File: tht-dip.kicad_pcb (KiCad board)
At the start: 2 copper layers, 100 x 49 mm, 56 parts, among them J1 Conn_01x01_Female, J10 Conn_01x01_Female, J2 Conn_01x01_Female, J3 Conn_01x01_Female, J4 Conn_01x01_Female, J5 Conn_01x01_Female, J6 Conn_01x01_Female, J7 Conn_01x01_Female, J8 Conn_01x01_Female, J9 Conn_01x01_Female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

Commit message: Add files via upload
updated files.
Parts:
- moved J8 1.00 mm to (39.0, 76.0), turned to 90 degrees

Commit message: Add files via upload
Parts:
- removed R19, R27: 8K, Resistor_THT:R_Axial_DIN0204_L3.6mm_D1.6mm_P5.08mm_Horizontal
- removed the REF** at (123.0, 70.2)
- added REF**: OSHW-Logo2_14.6x12mm_SilkScreen, Symbol:OSHW-Logo2_14.6x12mm_SilkScreen, F.Cu at (122.8, 69.5)
- R13, R21: value 2K -> 3K
- R14, R22: value 3K -> 4K
- R15, R23: value 4K -> 5K
- R16, R24: value 5K -> 6K
- R17, R25: value 6K -> 7K
- R18, R26: value 7K -> 8K
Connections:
- SW1 pad 9: Net-(R19-Pad2) -> (no net)
- SW2 pad 9: Net-(R27-Pad2) -> (no net)
- U1 pad 1: Net-(U1-Pad1) -> (no net)
- U1 pad 5: Net-(U1-Pad5) -> (no net)
- U1 pad 8: Net-(U1-Pad8) -> (no net)
- U2 pad 1: Net-(U2-Pad1) -> (no net)
- U2 pad 5: Net-(U2-Pad5) -> (no net)
- U2 pad 8: Net-(U2-Pad8) -> (no net)
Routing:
- net Net-(R27-Pad2): track 3.04 -> 0.00 mm
- net Net-(R19-Pad2): track 2.86 -> 0.00 mm
- net ResOUT: vias 0 -> 1

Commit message: Add files via upload
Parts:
- C3: footprint Capacitor_THT:C_Disc_D5.0mm_W2.5mm_P2.50mm -> Capacitor_THT:CP_Radial_D6.3mm_P2.50mm
- moved C3 45.2 mm to (114.5, 55.0), turned to 0 degrees
- moved REF** 0.50 mm to (123.2, 69.5)
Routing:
- net VCC: track 183.2 -> 187.7 mm
- net V-: track 202.5 -> 206.7 mm

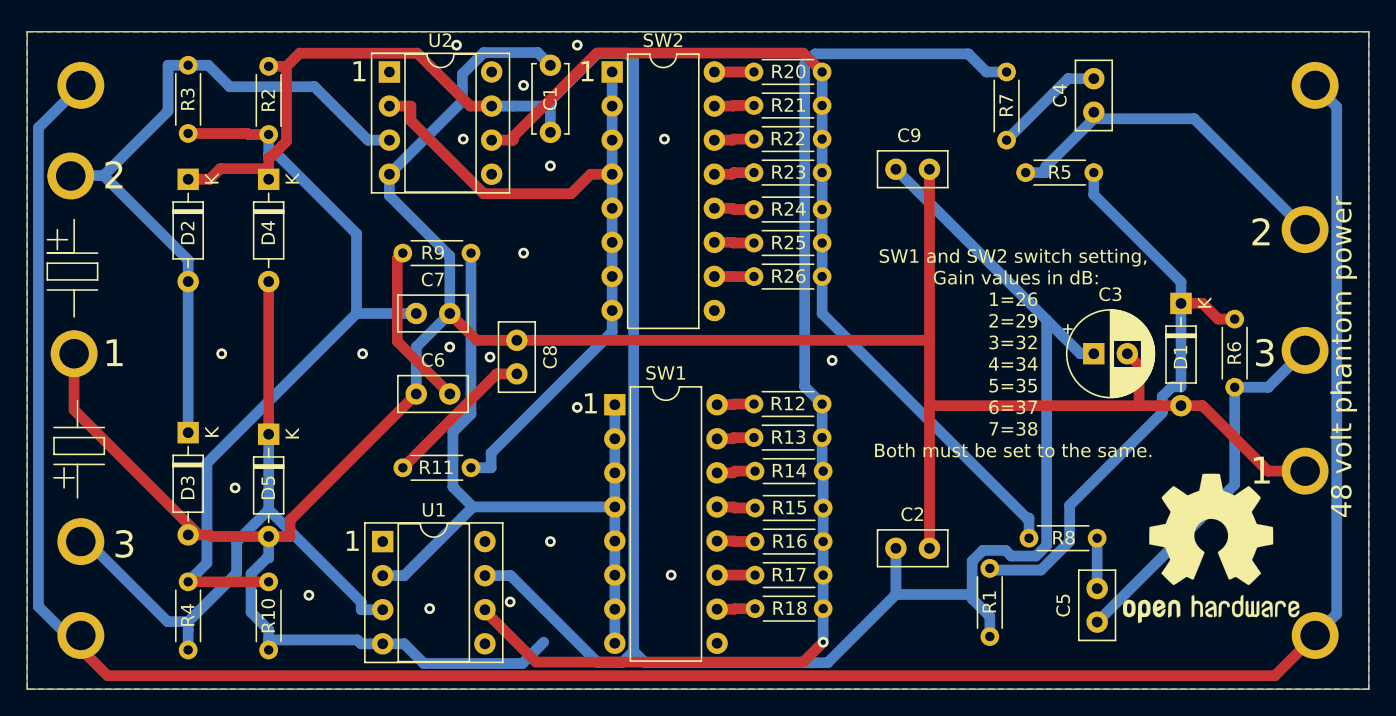
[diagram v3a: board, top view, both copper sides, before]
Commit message: Add files via upload
Updated, with the addition of a 700 ohm resistor.
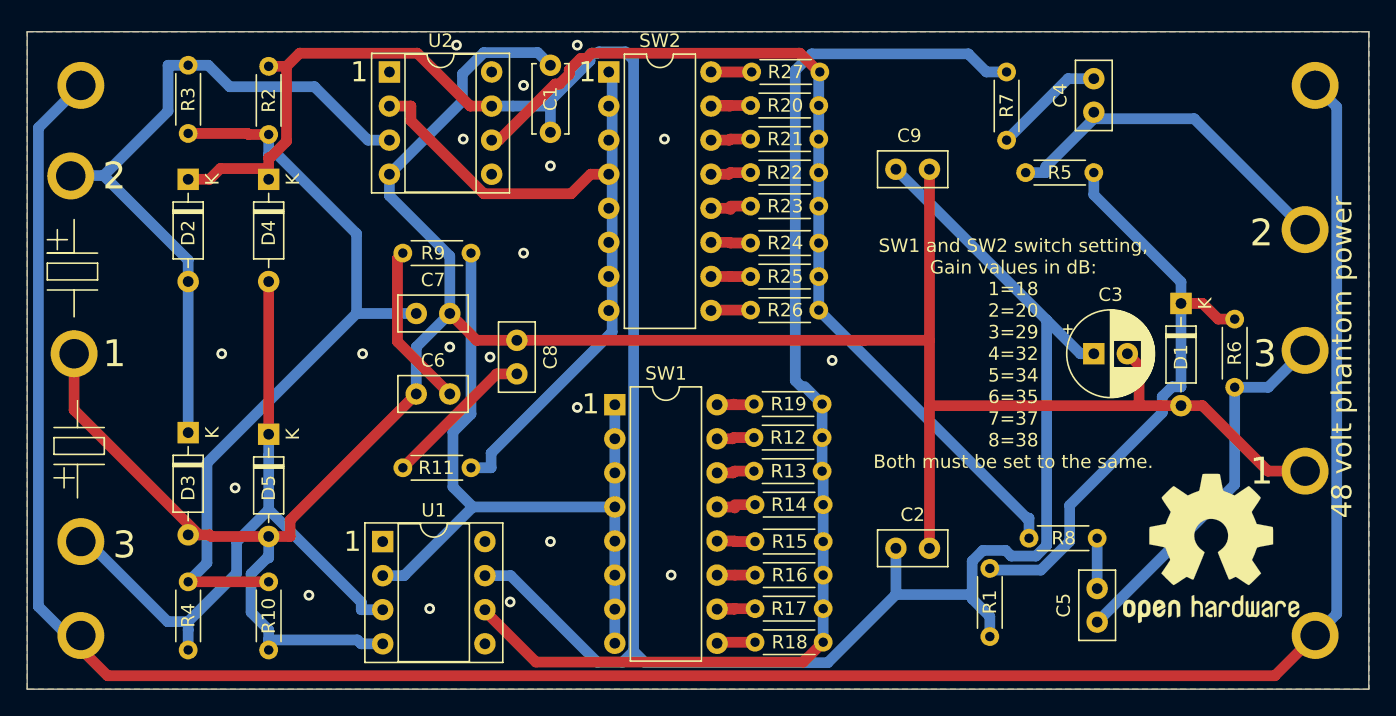
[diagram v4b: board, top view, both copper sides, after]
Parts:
- added R19: 700, Resistor_THT:R_Axial_DIN0204_L3.6mm_D1.6mm_P5.08mm_Horizontal, F.Cu at (94.2, 58.8)
- added R27: 700, Resistor_THT:R_Axial_DIN0204_L3.6mm_D1.6mm_P5.08mm_Horizontal, F.Cu at (94.1, 34.0)
- moved R20 2.51 mm to (94.0, 36.5)
- moved R21 2.51 mm to (94.0, 39.0)
- moved R22 2.51 mm to (94.0, 41.5)
- moved R23 2.51 mm to (94.0, 44.0)
- moved R24 2.51 mm to (94.0, 46.8)
- moved R25 2.51 mm to (94.0, 49.2)
- moved R26 2.51 mm to (94.0, 51.8)
- moved R12 2.50 mm to (94.2, 61.2)
- moved R13 2.50 mm to (94.2, 63.8)
- moved R14 2.50 mm to (94.3, 66.2)
- moved R15 2.50 mm to (94.3, 69.0)
- moved R16 2.50 mm to (94.3, 71.5)
- moved R17 2.50 mm to (94.3, 74.0)
- moved R18 2.50 mm to (94.3, 76.5)
- moved SW2 0.25 mm to (78.3, 34.0)
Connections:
- SW1 pad 10: Net-(R18-Pad2) -> Net-(R17-Pad2)
- SW1 pad 11: Net-(R17-Pad2) -> Net-(R16-Pad2)
- SW1 pad 12: Net-(R16-Pad2) -> Net-(R15-Pad2)
- SW1 pad 13: Net-(R15-Pad2) -> Net-(R14-Pad2)
- SW1 pad 14: Net-(R14-Pad2) -> Net-(R13-Pad2)
- SW1 pad 15: Net-(R13-Pad2) -> Net-(R12-Pad2)
- SW1 pad 16: Net-(R12-Pad2) -> Net-(R19-Pad2)
- SW1 pad 9: (no net) -> Net-(R18-Pad2)
- SW2 pad 10: Net-(R26-Pad2) -> Net-(R25-Pad2)
- SW2 pad 11: Net-(R25-Pad2) -> Net-(R24-Pad2)
- SW2 pad 12: Net-(R24-Pad2) -> Net-(R23-Pad2)
- SW2 pad 13: Net-(R23-Pad2) -> Net-(R22-Pad2)
- SW2 pad 14: Net-(R22-Pad2) -> Net-(R21-Pad2)
- SW2 pad 15: Net-(R21-Pad2) -> Net-(R20-Pad2)
- SW2 pad 16: Net-(R20-Pad2) -> Net-(R27-Pad2)
- SW2 pad 9: (no net) -> Net-(R26-Pad2)
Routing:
- net V-: track 206.7 -> 193.5 mm
- net Net-(R27-Pad2): track 0.00 -> 3.03 mm
- net Net-(R19-Pad2): track 0.00 -> 2.84 mm
- net Net-(R20-Pad2): track 2.95 -> 4.42 mm
- net Net-(R17-Pad2): track 2.83 -> 4.18 mm
- net ResOUT: track 87.1 -> 87.7 mm
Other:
- board text added: "SW1 and SW2 switch setting, Gain values in dB: 1=18 2=20 3=29 4=32 5=34 6=35 7=37 8=38 Both must be set to the same."
- board text removed: "SW1 and SW2 switch setting, Gain values in dB: 1=26 2=29 3=32 4=34 5=35 6=37 7=38 Both must be set to the same."

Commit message: Add files via upload
Changed to TL082BCP , less current use.
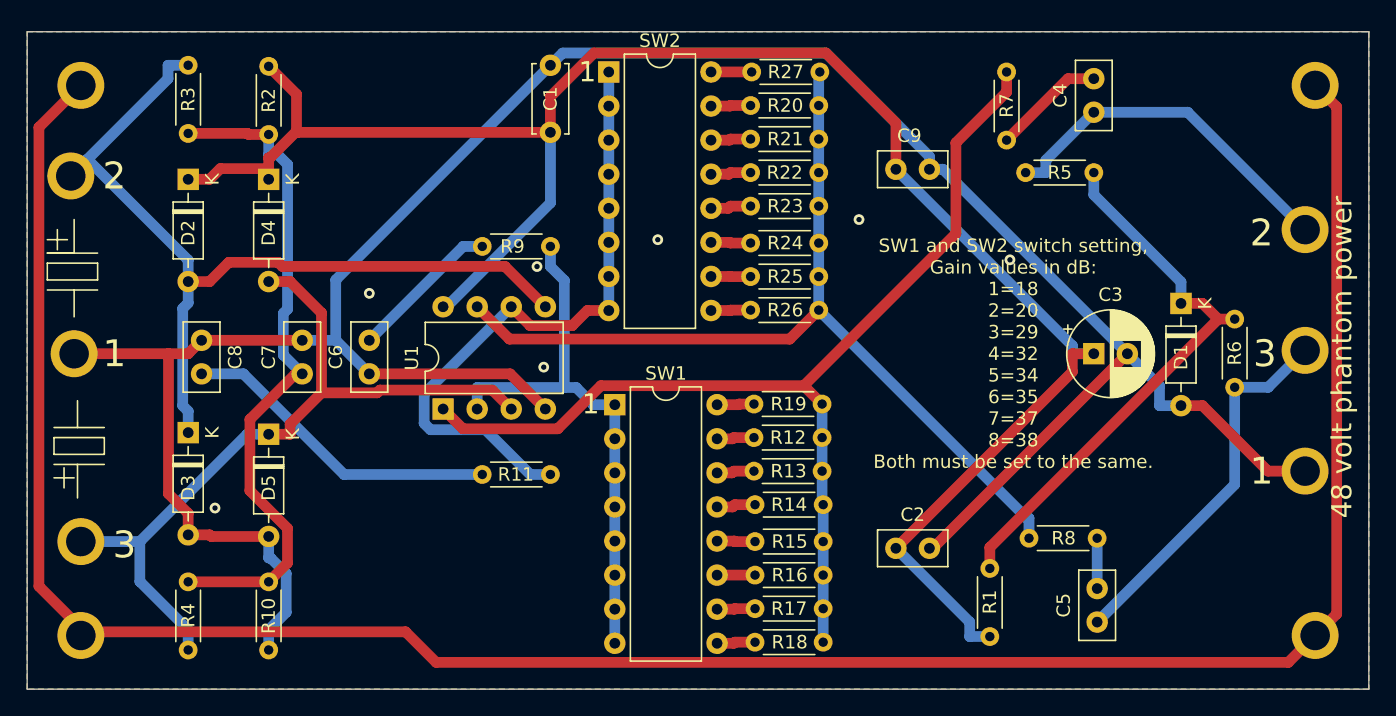
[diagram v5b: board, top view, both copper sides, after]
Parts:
- removed REF**: OSHW-Logo2_14.6x12mm_SilkScreen, Symbol:OSHW-Logo2_14.6x12mm_SilkScreen
- removed U2: NE5534, Package_DIP:DIP-8_W7.62mm_Socket
- D1: value 1N4746A (18V) -> 1N5241B-TR
- U1: value NE5534 -> TL082BCP; footprint Package_DIP:DIP-8_W7.62mm_Socket -> Package_DIP:DIP-8_W7.62mm
- moved C8 23.5 mm to (48.0, 54.0)
- moved U1 10.9 mm to (66.0, 59.1), turned to 90 degrees
- moved C7 9.62 mm to (55.5, 56.5), turned to 90 degrees
- moved R11 5.94 mm to (68.9, 64.0)
- moved R9 5.94 mm to (68.9, 47.0)
- moved C6 3.81 mm to (60.5, 56.5), turned to 90 degrees
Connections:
- U1 pad 1: (no net) -> ResOUT
- U1 pad 5: (no net) -> ind
- U1 pad 6: ResOUT -> ResIN1
- U1 pad 7: VCC -> ResOUT2
- U1 pad 8: (no net) -> VCC
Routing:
- net VCC: track 188.1 -> 140.0 mm
- net ResIN: track 57.3 -> 41.1 mm
- net Net-(C8-Pad2): track 11.4 -> 24.0 mm
- net ind: track 53.3 -> 65.2 mm
- net ResOUT: track 87.7 -> 78.2 mm, vias 1 -> 0
- net Net-(C7-Pad1): track 58.1 -> 50.7 mm
- net V-: track 193.5 -> 186.3 mm
- net ResIN1: track 55.3 -> 48.5 mm
- net Net-(D4-Pad2): track 53.2 -> 58.2 mm
- net Net-(D1-Pad1): track 45.4 -> 42.6 mm
- net Net-(R20-Pad2): track 4.42 -> 2.97 mm
- net Earth: track 181.0 -> 179.6 mm, vias 19 -> 7
- net Net-(R17-Pad2): track 4.18 -> 2.85 mm
- net Net-(C6-Pad2): track 12.3 -> 11.3 mm

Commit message: Add files via upload
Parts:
- removed R12, R20: 1K, Resistor_THT:R_Axial_DIN0204_L3.6mm_D1.6mm_P5.08mm_Horizontal
- removed R13, R21: 3K, Resistor_THT:R_Axial_DIN0204_L3.6mm_D1.6mm_P5.08mm_Horizontal
- removed R14, R22: 4K, Resistor_THT:R_Axial_DIN0204_L3.6mm_D1.6mm_P5.08mm_Horizontal
- removed R15, R23: 5K, Resistor_THT:R_Axial_DIN0204_L3.6mm_D1.6mm_P5.08mm_Horizontal
- removed R16, R24: 6K, Resistor_THT:R_Axial_DIN0204_L3.6mm_D1.6mm_P5.08mm_Horizontal
- removed R17, R25: 7K, Resistor_THT:R_Axial_DIN0204_L3.6mm_D1.6mm_P5.08mm_Horizontal
- removed R18, R26: 8K, Resistor_THT:R_Axial_DIN0204_L3.6mm_D1.6mm_P5.08mm_Horizontal
- removed R19, R27: 700, Resistor_THT:R_Axial_DIN0204_L3.6mm_D1.6mm_P5.08mm_Horizontal
- removed SW1, SW2: JS0108AP4-S, Package_DIP:DIP-16_W7.62mm
- added RV1: R_Potentiometer_Dual, potmeter:PTD902-2015K-B103, F.Cu at (87.0, 56.5)
- C1: renamed from C9; footprint Capacitor_THT:C_Disc_D5.0mm_W2.5mm_P2.50mm -> Capacitor_THT:CP_Radial_D5.0mm_P2.00mm
- C7: renamed from C6; footprint Capacitor_THT:C_Disc_D5.0mm_W2.5mm_P2.50mm -> Capacitor_THT:CP_Radial_D5.0mm_P2.00mm
- C9: renamed from C8; footprint Capacitor_THT:C_Disc_D5.0mm_W2.5mm_P2.50mm -> Capacitor_THT:CP_Radial_D5.0mm_P2.00mm
- moved C4 17.0 mm to (99.5, 63.0)
- moved C9 15.1 mm to (60.5, 62.5)
- moved C7 8.50 mm to (60.5, 48.0)
- moved C1 4.37 mm to (100.0, 45.0), turned to 0 degrees
- moved C3 4.01 mm to (99.5, 73.5)
- renumbered C1 to C2, C2 to C3, C3 to C4, C4 to C5, C5 to C6, C7 to C8
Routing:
- net Earth: track 179.6 -> 0.00 mm, vias 7 -> 12
- net V-: track 186.3 -> 208.9 mm
- net VCC: track 140.0 -> 120.7 mm
- net ResOUT2: track 68.7 -> 52.5 mm
- net ResOUT: track 78.2 -> 93.7 mm
- net Net-(C9-Pad2): track 24.0 -> 8.63 mm
- net ResIN1: track 48.5 -> 34.6 mm
- net Net-(D4-A): track 58.2 -> 70.9 mm
- net ResIN: track 41.1 -> 44.7 mm
- net Net-(R27-Pad2): track 3.03 -> 0.00 mm
- net Net-(R23-Pad2): track 3.02 -> 0.00 mm
- net Net-(R22-Pad2): track 3.00 -> 0.00 mm
- net Net-(R21-Pad2): track 2.98 -> 0.00 mm
- net Net-(R24-Pad2): track 2.97 -> 0.00 mm
- net Net-(R20-Pad2): track 2.97 -> 0.00 mm
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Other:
- net class Default removed
- board text removed: "SW1 and SW2 switch setting, Gain values in dB: 1=18 2=20 3=29 4=32 5=34 6=35 7=37 8=38 Both must be set to the same."
